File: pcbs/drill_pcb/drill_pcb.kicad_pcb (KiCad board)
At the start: 2 copper layers, 105 x 103 mm, 47 parts, among them J1 24V IN, J10 LIMIT SWITCH BOTTOM, J11 DEEP WEIGHT SENSOR, J12 SURFACE WEIGHT SENSOR, J13 SERVO 1, J14 SERVO 2, J15 STEPPER STORAGE, J2 uC COMMUNICATION, J3 ENCODER VERTICAL DRIVE, J4 LIMIT SWITCH TOP, J5 HEIGHT SENSOR, J6 STEPPER VERTICAL DRIVE, J7 DC MOTOR 24 V, J8 DC MOTOR UART, J9 ENCODER STORAGE, Q1 PMOS, U1 ESP32-DevKitC, U2 LM3940, U3 INA219BxD

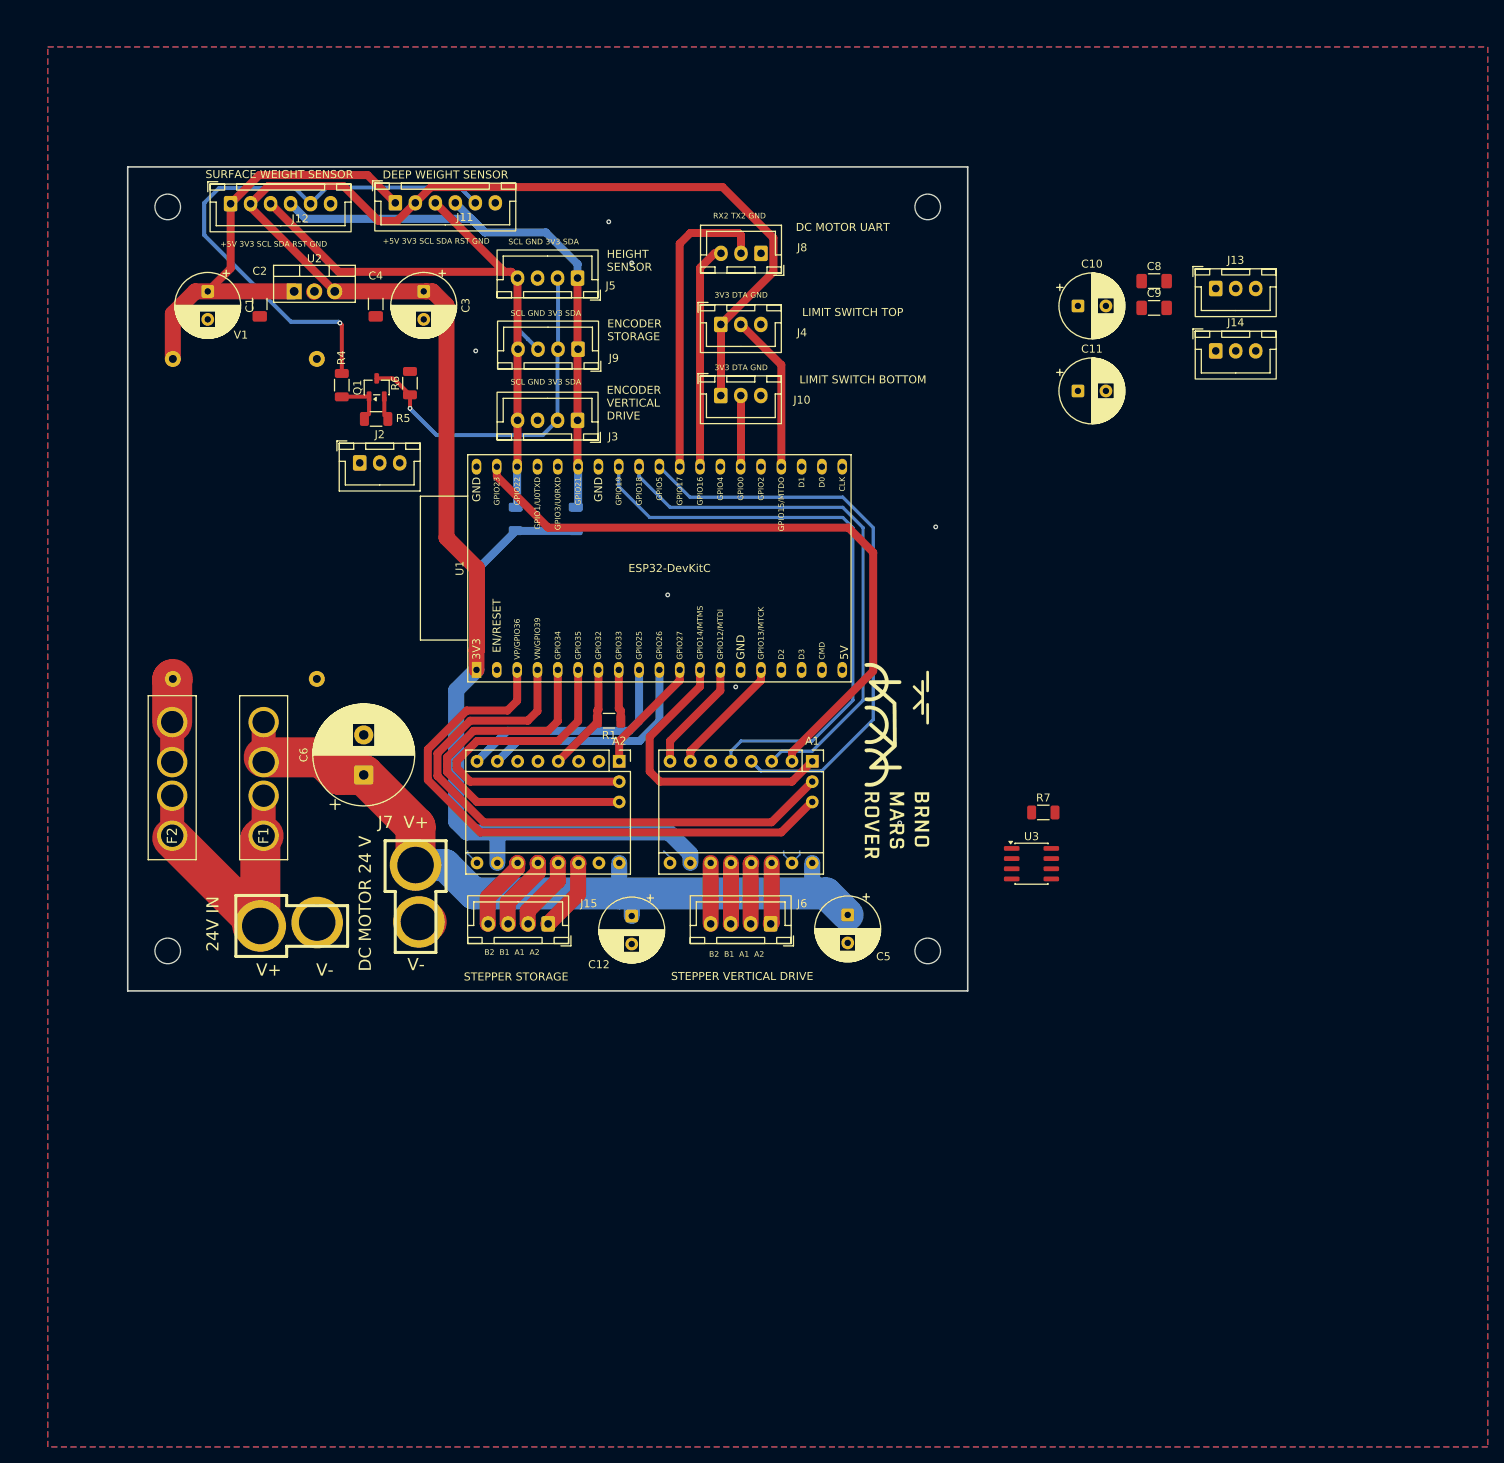
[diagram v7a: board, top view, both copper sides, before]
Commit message: Board 1.2 ready; drc errors none
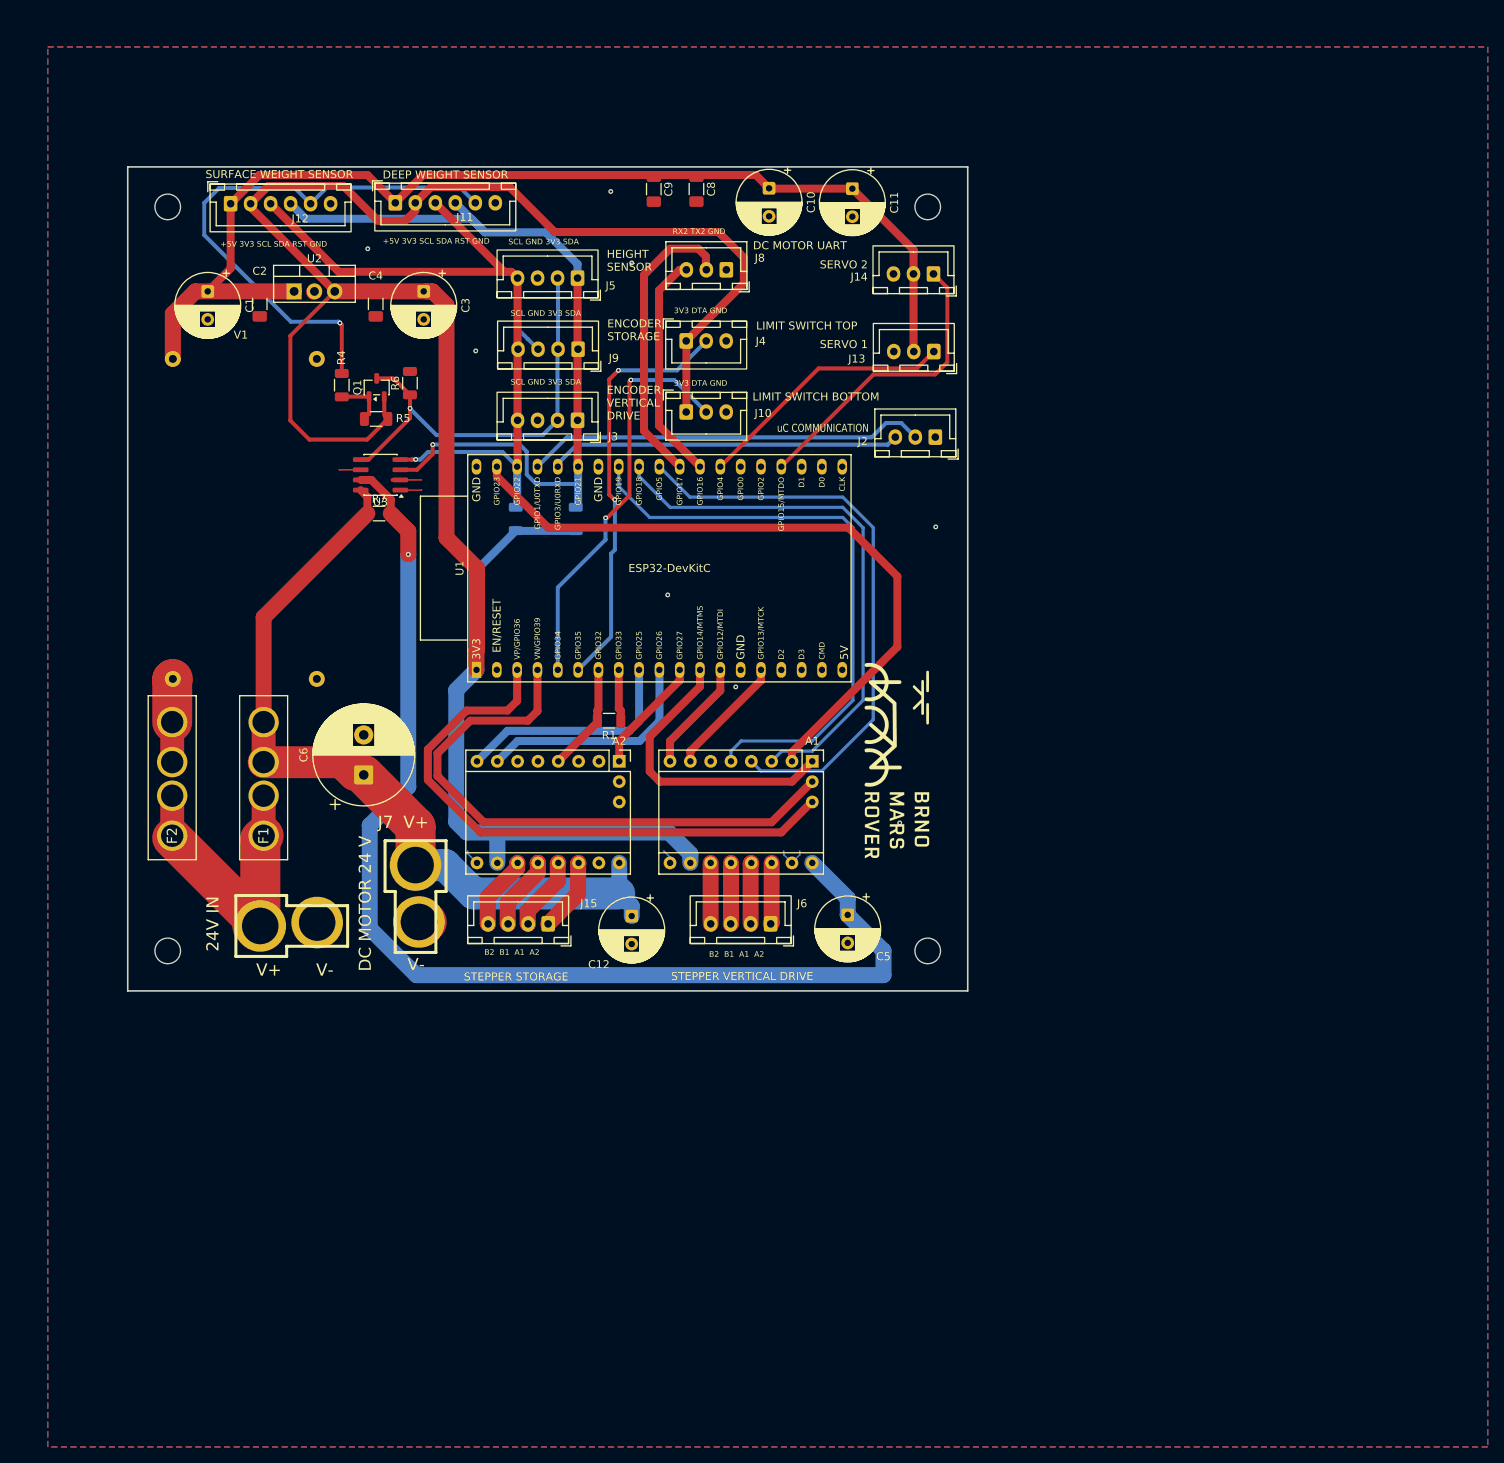
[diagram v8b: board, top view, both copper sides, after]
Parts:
- moved U3 94.8 mm to (61.6, 78.5), turned to 180 degrees
- moved R7 91.0 mm to (61.4, 83.3)
- moved J2 72.0 mm to (130.9, 73.8), turned to 180 degrees
- moved C9 64.3 mm to (95.8, 42.8), turned to -90 degrees
- moved C8 58.4 mm to (101.1, 42.8), turned to -90 degrees
- moved C10 41.3 mm to (110.2, 42.7), turned to -90 degrees
- moved C11 37.9 mm to (120.6, 42.7), turned to -90 degrees
- moved J14 36.6 mm to (130.7, 53.4), turned to 180 degrees
- moved J13 36.1 mm to (130.8, 63.1), turned to 180 degrees
- moved J10 4.80 mm to (99.8, 70.6)
- moved J4 4.80 mm to (99.8, 61.8)
- moved J8 4.80 mm to (104.8, 52.9)
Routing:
- net Net-(A1-VM): track 0.00 -> 145.9 mm, vias 0 -> 1
- net +5V: track 57.6 -> 140.4 mm
- net LIMIT_SWITCH_TOP: track 0.00 -> 52.7 mm, vias 0 -> 2
- net LIMIT_SWITCH_BOTTOM: track 0.00 -> 51.2 mm, vias 0 -> 2
- net TX0: track 0.00 -> 50.2 mm
- net unconnected-(A2-DIAG1-Pad18): track 47.0 -> 0.00 mm
- net unconnected-(A2-DIAG0-Pad17): track 45.5 -> 0.00 mm
- net RX0: track 0.00 -> 43.9 mm
- net SERVO2_PWM: track 0.00 -> 37.9 mm
- net SERVO1_PWM: track 0.00 -> 32.6 mm
- net +3.3V: track 257.9 -> 288.3 mm
- net SDA1: track 75.3 -> 103.3 mm, vias 0 -> 1
- net (no net): track 19.9 -> 0.00 mm
- net SCL1: track 75.9 -> 91.7 mm, vias 0 -> 1
- net +3.3VP: track 45.2 -> 54.7 mm
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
